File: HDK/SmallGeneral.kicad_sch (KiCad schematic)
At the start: 39 parts, among them J104 Conn_01x08, J109 Conn_01x08, J401 USB_C, J405 PH_01x05V-H, J406 PH_01x05V-H, J407 PH_01x05V-H, J414 PHD_02x04V-H, SW401 SW_Push, SW402 SW_Push, U101 STM32F072CBTx, U201 AMS1117-3.3, U402 TJA1042T-3

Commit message: updated rev3
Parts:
- removed J104, J109: Conn_01x08, Connector_PinHeader_2.54mm:PinHeader_1x08_P2.54mm_Vertical, symbol Connector_Generic:Conn_01x08
- removed J405, J406, J407: PH_01x05V-H, NVF-Kicad:PH_01x05H-H, symbol Connector_Generic:Conn_01x05
- removed J414 (x3): PHD_02x04V-H, NVF-Kicad:PHD_02x04H-H, symbol Connector_Generic:Conn_02x04_Odd_Even
- removed R302: 10k, Resistor_SMD:R_0603_1608Metric, symbol Device:R
- removed SWD101: SWD_Breakout_Minimal, NVF-Kicad:PH_01x05H-H, symbol NVF-Kicad:SWD_Breakout_Minimal
- added C201, C202: 2u2, Capacitor_SMD:C_0805_2012Metric, symbol Device:C
- added C401: 100n, Capacitor_SMD:C_0603_1608Metric, symbol Device:C
- added D101: GREEN, LED_SMD:LED_0603_1608Metric, symbol Device:LED
- added D102: RED, LED_SMD:LED_0603_1608Metric, symbol Device:LED
- added D103: BLUE, LED_SMD:LED_0603_1608Metric, symbol Device:LED
- added R105, R106, R107: 200, Resistor_SMD:R_0603_1608Metric, symbol Device:R
- added R406 (x2): 1k, Resistor_SMD:R_0603_1608Metric, symbol Device:R
- added R406 (x3): 10k, Resistor_SMD:R_0603_1608Metric, symbol Device:R
- added RV102: 10k, NVF-Kicad:RV_Bourns_3362, symbol Device:R_Potentiometer
- added SG101: ~, NVF-OwnParts:Small-General Actual, symbol NVF-Kicad:SmallGeneral
- added SW401: SW_Push, NVF-Kicad:PushBtn_TS-1187A-B-A-B, symbol Switch:SW_Push
- added TP102, TP103: TestPoint, TestPoint:TestPoint_Pad_2.5x2.5mm, symbol Connector:TestPoint
- added U104: AMS1117-5.0, Package_TO_SOT_SMD:SOT-223-3_TabPin2, symbol Regulator_Linear:AMS1117-5.0
- renumbered C105 to C102, C102 to C105
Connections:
- net +3V3: now also D102.2 (A), D103.2 (A), R406.1, R406.1, SG101.C2 (3V3), SG101.D2 (3V3), SG101.E2 (3V3), SG101.F2 (3V3), SG101.G1 (3V3)
- net +5V: now also C202.1, D101.2 (A), SG101.C1 (5V), SG101.D1 (5V), SG101.E1 (5V), SG101.F1 (5V), U104.2 (VO)
- net A0: now also SG101.C3 (A0)
- net A0_MCU: now also U101.10 (PA0); no longer U101.11 (PA1)
- net CAN_H: now also SG101.A8 (CAN_H), SG101.B8 (CAN_H), SG101.L8 (CAN_H)
- net CAN_L: now also SG101.A7 (CAN_L), SG101.B7 (CAN_L), SG101.L7 (CAN_L)
- net GND: now also C201.2, C202.2, C401.2, R105.2, R106.2, R406.2, RV102.3, SG101.A2 (GND), SG101.A4 (GND), SG101.B2 (GND), SG101.B4 (GND), SG101.C5 (GND), SG101.D5 (GND), SG101.E4 (GND), SG101.F5 (GND), SG101.G4 (GND), SG101.L2 (GND), SG101.L4 (GND), SW401.2, TP103.1, U104.1 (GND)
- net I2C_SCL: now also SG101.F3 (I2C_SCL)
- net I2C_SDA: now also SG101.F4 (I2C_SDA)
- net NRST: now also R406.2, SG101.G5 (NRST)
- net PA8: now also SG101.R3 (PA8)
- net PB11: now also SG101.R8 (PB11)
- net PB12: now also SG101.R7 (PB12)
- net PB13: now also SG101.R6 (PB13)
- net PB14: now also SG101.R5 (PB14)
- net PB15: now also SG101.R4 (PB15)
- net SPI_CS: now also SG101.E8 (SPI_CS)
- net SPI_IRQ: now also SG101.E3 (SPI_IRQ)
- net SPI_MISO: now also SG101.E6 (SPI_MISO)
- net SPI_MOSI: now also SG101.E7 (SPI_MOSI)
- net SPI_SCLK: now also SG101.E5 (SPI_SCLK)
- net SWCLK: now also SG101.G3 (SWCLK)
- net SWDIO: now also SG101.G2 (SWDIO)
- net UART2_RX: now also SG101.D4 (UART_RX)
- net UART2_TX: now also SG101.D3 (UART_TX)
- net UART_RX: now also SG101.R1 (PA10)
- net UART_TX: now also SG101.R2 (PA9)
- net V1: now also SG101.A1 (V1), SG101.B1 (V1), SG101.L1 (V1)
- net V2: now also SG101.A3 (V2), SG101.B3 (V2), SG101.L3 (V2)
- net VCC: now also C201.1, R406.1, U104.3 (VI)
- net V_{SENSE}: now reaches U101.19 (PB1)
- net V_{SENSE}: now also R406.1, R406.2
- net USR_BTN: now reaches U101.20 (PB2)
- net USR_BTN: now also C401.1, R406.1, R406.2
- net USR_LED: now reaches U101.21 (PB10)
- net USR_LED: now also R107.2
- new net: D102.1 (K), R106.1
- new net: R406.2, SW401.1
- new net: D103.1 (K), R107.1
- new net: D101.1 (K), R105.1
- new net A1: RV102.1, SG101.C4 (A1)
- new net A1_MCU: RV102.2, TP102.1, U101.11 (PA1)
- no-connect marks 19 -> 10
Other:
- note added: "Analog Signal Calibration"
- note added: "Assuming conditions: LED: V_{F}: 2.5V, I_{F}: 4mA Calculations for CLR: 3v3-2v5=0v8 V=IR: 0v8 = 0.04R R = 200"
- note added: "BOOT0 Default Pull-Down"
- note added: "Board Connectors A"
- note added: "Board Connectors B"
- note added: "Div Factor 1/11"
- note added: "MCU"
- note added: "MCU Decoupling"
- note added: "Power Merge"
- note added: "Power/User Indicators + User Button"
- note added: "RCC Circuitry"
- note added: "Ref: CLR Calculator"
- note added: "Ref: STM32 Pin Current MAX MCU MAX I_{IO(PIN)} = 25mA,"
- note added: "TestPoints for: A0, A1, GND are used for probing A0, A1 voltage diviiding factor to ensure V_{Sense} for ADC is within Safe Range"
- note added: "USB C CC: 5k1 sink for 5V3A"
- note added: "V_{REG} - MCU 5.0V"
- note added: "~{NRST} Debounce"
- note added: "~{USR_BTN} Debounce"
- moved on the sheet: C102, C103, C104, C105, C201, C202, C401, C409, C410, D401, H103, H104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

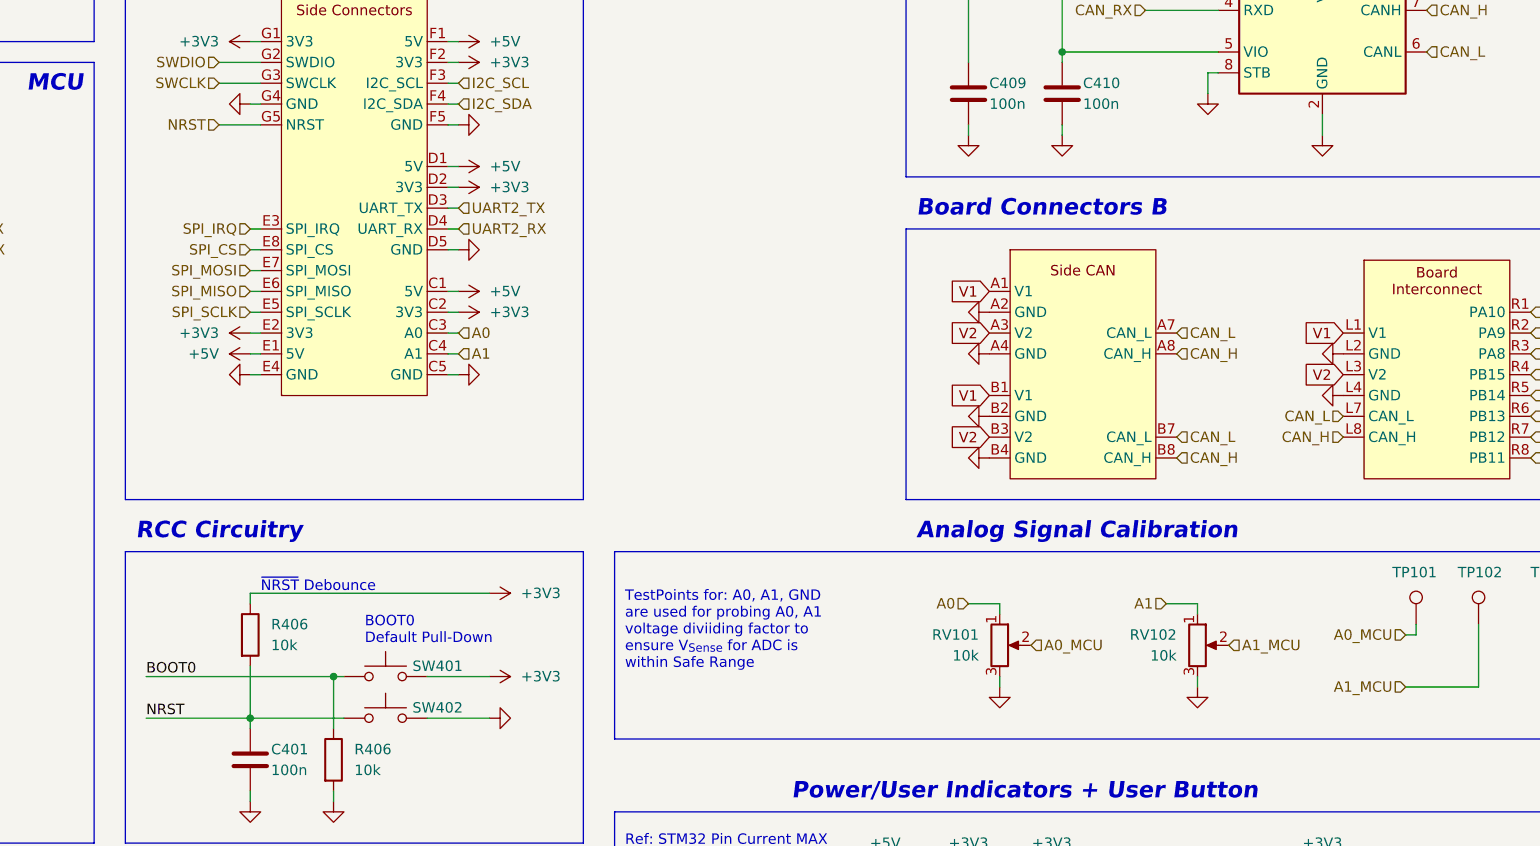
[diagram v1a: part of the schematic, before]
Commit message: updated Trim Pot Switch
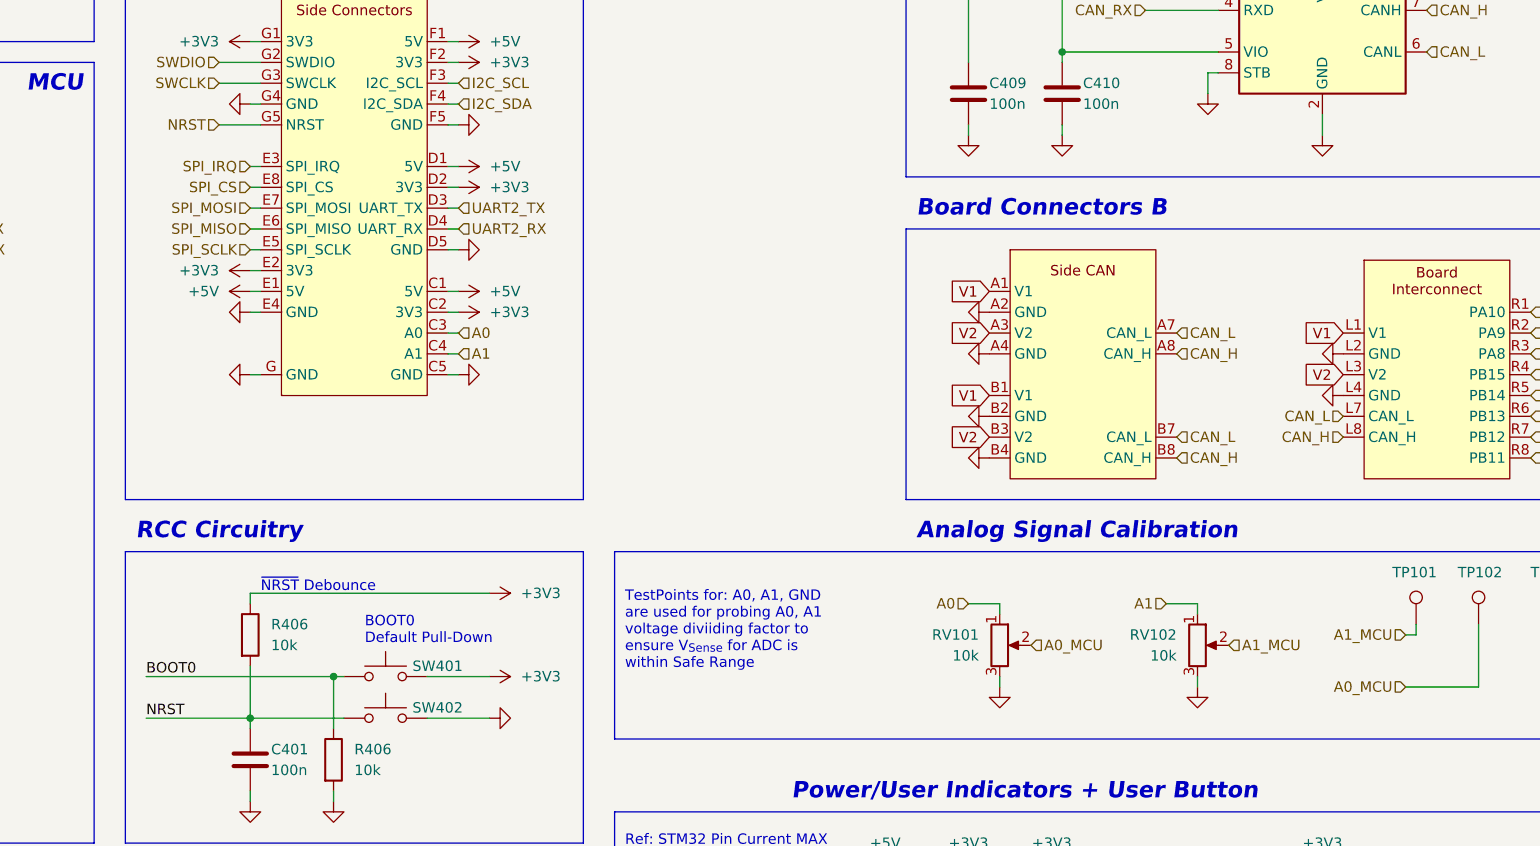
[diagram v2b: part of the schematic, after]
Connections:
- net A0_MCU: now also TP102.1; no longer TP101.1
- net A1_MCU: now also TP101.1; no longer TP102.1
- net GND: now also SG101.G (GND)

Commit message: updated  docs
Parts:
- removed H101, H102, H103, H104: MountingHole_Pad, -, symbol Mechanical:MountingHole_Pad
- added F101: Fuse, NVF-Kicad:FUSE-Littelfuse_Nano2_154x, symbol Device:Fuse
- D101: LCSC (none) -> C434423
- D102: LCSC (none) -> C2286
- D103: LCSC (none) -> C965807
- R105, R106, R107: LCSC (none) -> C8218
- R406: LCSC (none) -> C25804
- SG101: symbol NVF-Kicad:SmallGeneral -> NVF_OwnParts:SmallGeneral; LCSC (none) -> -
- U104: LCSC (none) -> C6187
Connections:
- net +3V3: now also SG101.E7 (SPI_MOSI); no longer SG101.E2 (3V3)
- net +5V: now also SG101.E6 (SPI_MISO); no longer SG101.E1 (5V)
- net GND: now also SG101.E5 (SPI_SCLK); no longer SG101.G (GND)
- net SPI_CS: no longer SG101.E8 (SPI_CS)
- net SPI_IRQ: no longer SG101.E3 (SPI_IRQ)
- net SPI_MISO: now also SG101.E3 (SPI_IRQ); no longer SG101.E6 (SPI_MISO)
- net SPI_MOSI: no longer SG101.E7 (SPI_MOSI)
- net SPI_SCLK: now also SG101.E8 (SPI_CS); no longer SG101.E5 (SPI_SCLK)
- net VCC: now also F101.2; no longer D401.1 (K), D401.1 (K)
- new net: D401.1 (K), D401.1 (K), F101.1
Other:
- moved on the sheet: D401

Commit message: updated rev4
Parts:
- R406: LCSC C25804 -> C21190
- U101: value STM32F072CBTx -> STM32F072CBT6
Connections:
- net +3V3: now also SG101.E2 (3V3); no longer SG101.E7 (SPI_MOSI)
- net +5V: now also SG101.E1 (5V); no longer SG101.E6 (SPI_MISO)
- net GND: no longer SG101.E5 (SPI_SCLK)
- net SPI_CS: now also SG101.E8 (SPI_CS)
- net SPI_IRQ: now also SG101.E3 (SPI_IRQ)
- net SPI_MISO: now also SG101.E6 (SPI_MISO); no longer SG101.E3 (SPI_IRQ)
- net SPI_MOSI: now also SG101.E7 (SPI_MOSI)
- net SPI_SCLK: now also SG101.E5 (SPI_SCLK); no longer SG101.E8 (SPI_CS)
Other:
- moved on the sheet: D401, RV101, RV102

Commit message: updated rev4.1
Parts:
- added JP101: Jumper_2_Open, Connector_PinHeader_2.54mm:PinHeader_1x02_P2.54mm_Vertical, symbol Jumper:Jumper_2_Open
- C101, C102, C103, C104, C105, C106, C201, C202, C401, C409, C410, D101, D102, D103, D401, F101, J401, R401, R402, R406, RV101, RV102, SW401, SW402, U101, U104, U201, U402: Assemble (none) -> 1
- R105, R106, R107: value 200 -> 300; Assemble (none) -> 1; LCSC C8218 -> C23025
- SG101, TP101, TP102, TP103: Assemble (none) -> 0
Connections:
- net +5V: now also JP101.2 (B)
- net GND: now also SG101.L6 (GND)
- net VBUS: now also JP101.1 (A)
- net VCC: now also SG101.L5 (VCC)
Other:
- note added: "Bypass V_{USB}"
- moved on the sheet: D102, D103, D401, F101, R106, R107
